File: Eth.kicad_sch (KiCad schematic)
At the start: 0 parts

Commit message: Eth güncellendi.
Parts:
- added C18, C19: 22pF, symbol Device:C
- added C20: 22uF, symbol Device:C
- added C21, C22, C23: 0.1uF, symbol Device:C
- added J2: RJ45_Hanrun_HR911105A_Horizontal, Connector_RJ:RJ45_Hanrun_HR911105A_Horizontal, symbol Connector:RJ45_Hanrun_HR911105A_Horizontal
- added R3: 10k, symbol Device:R
- added R4: 6.49k, symbol Device:R
- added U3: KSZ8081RNA, Package_DFN_QFN:QFN-24-1EP_4x4mm_P0.5mm_EP2.6x2.6mm, symbol Interface_Ethernet:KSZ8081RNA
- added Y1: Crystal, symbol Device:Crystal
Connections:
- new net: C22.1, J2.5 (RCT)
- new net: C18.1, U3.7 (XO), Y1.1
- new net: C23.1, J2.4 (TCT)
- new net: C19.1, U3.8 (XI), Y1.2
- new net: C20.2, C21.2, U3.1 (VDD_1.2)
- new net: J2.6 (RD-), U3.3 (RXM)
- new net: J2.3 (RD+), U3.4 (RXP)
- new net: J2.2 (TD-), U3.5 (TXM)
- new net: J2.1 (TD+), U3.6 (TXP)
- new net: R4.1, U3.9 (REXT)
- new net +3V3: R3.1
- new net ETH_CRS_DV: R3.2, U3.15 (CRS_DV/PHYAD[1:0])
- new net ETH_MDC: U3.11 (MDC)
- new net ETH_MDIO: U3.10 (MDIO)
- new net ETH_REF_CLK: U3.16 (REF_CLK)
- new net ETH_RXD0: U3.13 (RXD0)
- new net ETH_RXD1: U3.12 (RXD1)
- new net ETH_TXD0: U3.20 (TXD0)
- new net ETH_TXD1: U3.21 (TXD1)
- new net ETH_TXEN: U3.19 (TXEN)
- new net GND: C18.2, C19.2, C20.1, C21.1, C22.2, C23.2, R4.2, U3.22 (GND), U3.25 (GND)

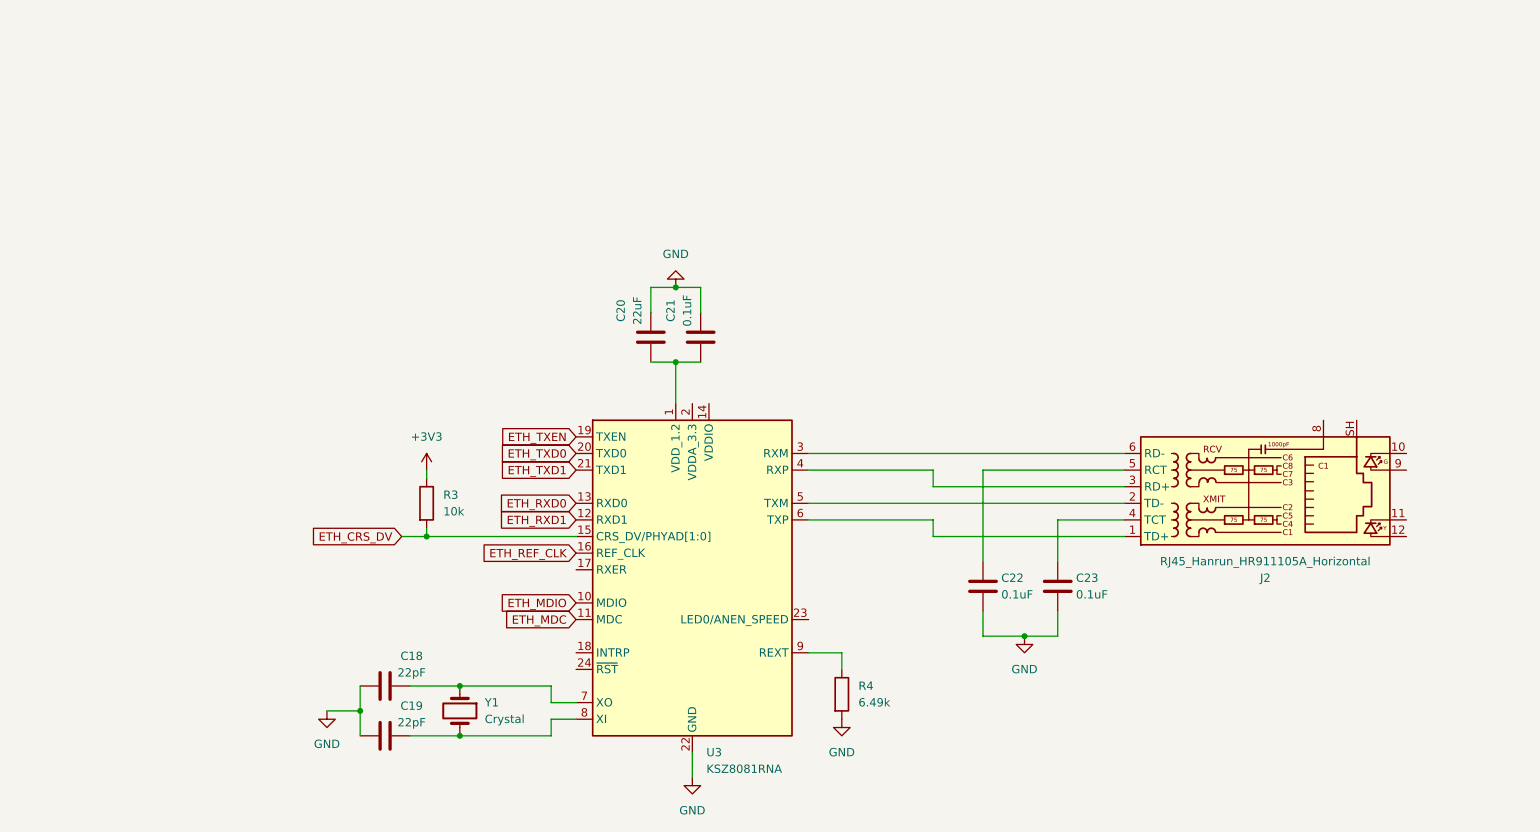
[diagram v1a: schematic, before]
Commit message: Eth güncellendi.
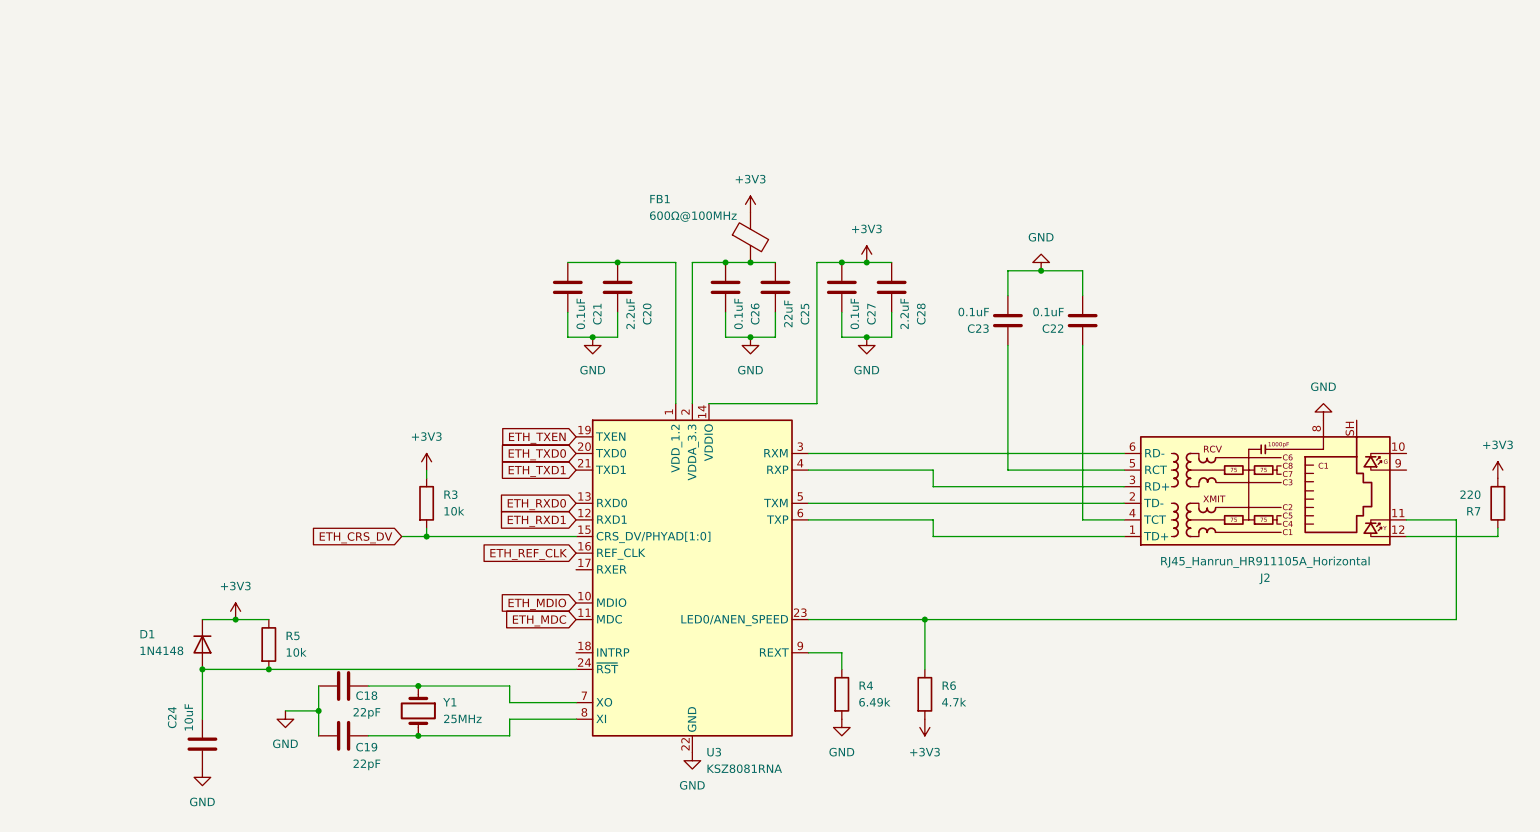
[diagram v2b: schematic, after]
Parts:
- added C24: 10uF, symbol Device:C
- added C25: 22uF, symbol Device:C
- added C26, C27: 0.1uF, symbol Device:C
- added C28: 2.2uF, symbol Device:C
- added D1: 1N4148, Diode_THT:D_DO-35_SOD27_P7.62mm_Horizontal, symbol Diode:1N4148
- added FB1: 600Ω@100MHz, symbol Device:FerriteBead
- added R5: 10k, symbol Device:R
- added R6: 4.7k, symbol Device:R
- added R7: 220, symbol Device:R
- C20: value 22uF -> 2.2uF
- Y1: value Crystal -> 25MHz
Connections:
- net +3V3: now also U3.14 (VDDIO), C27.2, C28.2, D1.1 (K), FB1.1, R5.1, R6.2, R7.2
- net GND: now also J2.8, C24.2, C25.1, C26.1, C27.1, C28.1
- net at C22.1: now also J2.4 (TCT); no longer J2.5 (RCT)
- net at C23.1: now also J2.5 (RCT); no longer J2.4 (TCT)
- net at U3.2 (VDDA_3.3): now also C25.2, C26.2, FB1.2
- net at U3.23 (LED0/ANEN_SPEED): now also J2.11, R6.1
- net at U3.24 (~{RST}): now also C24.1, D1.2 (A), R5.2
- net at J2.12: now also R7.1
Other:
- moved on the sheet: C18, C19, C20, C21, C22, C23, Y1

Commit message: Eth güncellendi.
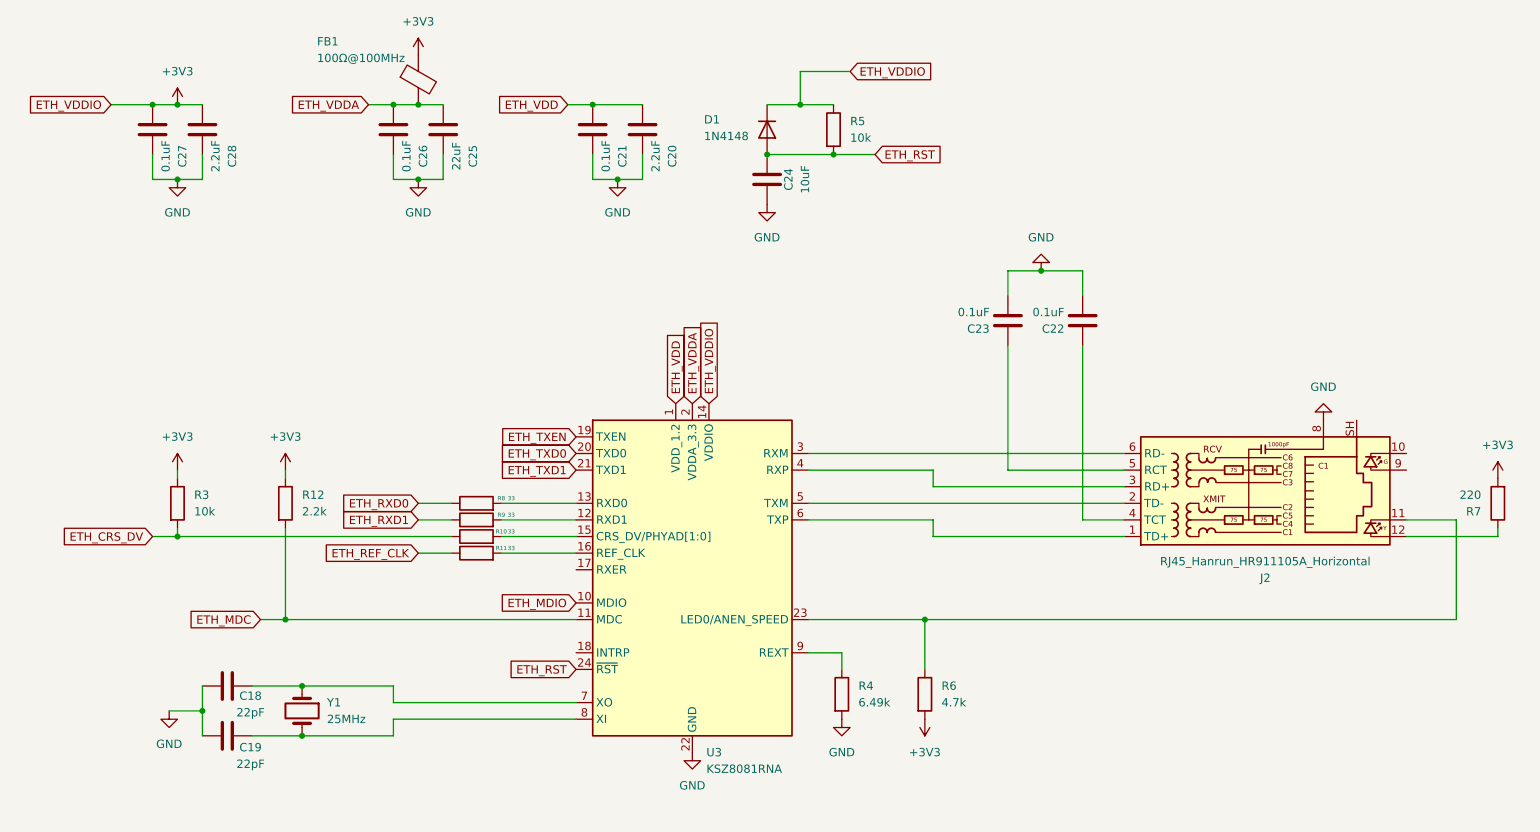
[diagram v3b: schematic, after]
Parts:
- added R10, R11, R8, R9: 33, symbol Device:R
- added R12: 2.2k, symbol Device:R
- FB1: value 600Ω@100MHz -> 100Ω@100MHz
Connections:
- net +3V3: now also R12.1
- net ETH_CRS_DV: now also R10.1; no longer U3.15 (CRS_DV/PHYAD[1:0])
- net ETH_MDC: now also R12.2
- net ETH_REF_CLK: now also R11.1; no longer U3.16 (REF_CLK)
- net ETH_RXD0: now also R8.1; no longer U3.13 (RXD0)
- net ETH_RXD1: now also R9.1; no longer U3.12 (RXD1)
- net ETH_VDDA: now reaches C25.2, C26.2, FB1.2, U3.2 (VDDA_3.3)
- net ETH_VDD: now reaches C20.2, C21.2, U3.1 (VDD_1.2)
- net ETH_RST: now reaches C24.1, D1.2 (A), R5.2, U3.24 (~{RST})
- new net: R9.2, U3.12 (RXD1)
- new net: R8.2, U3.13 (RXD0)
- new net: R10.2, U3.15 (CRS_DV/PHYAD[1:0])
- new net: R11.2, U3.16 (REF_CLK)
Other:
- moved on the sheet: C18, C19, R3, Y1

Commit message: Usb düzenlendi.
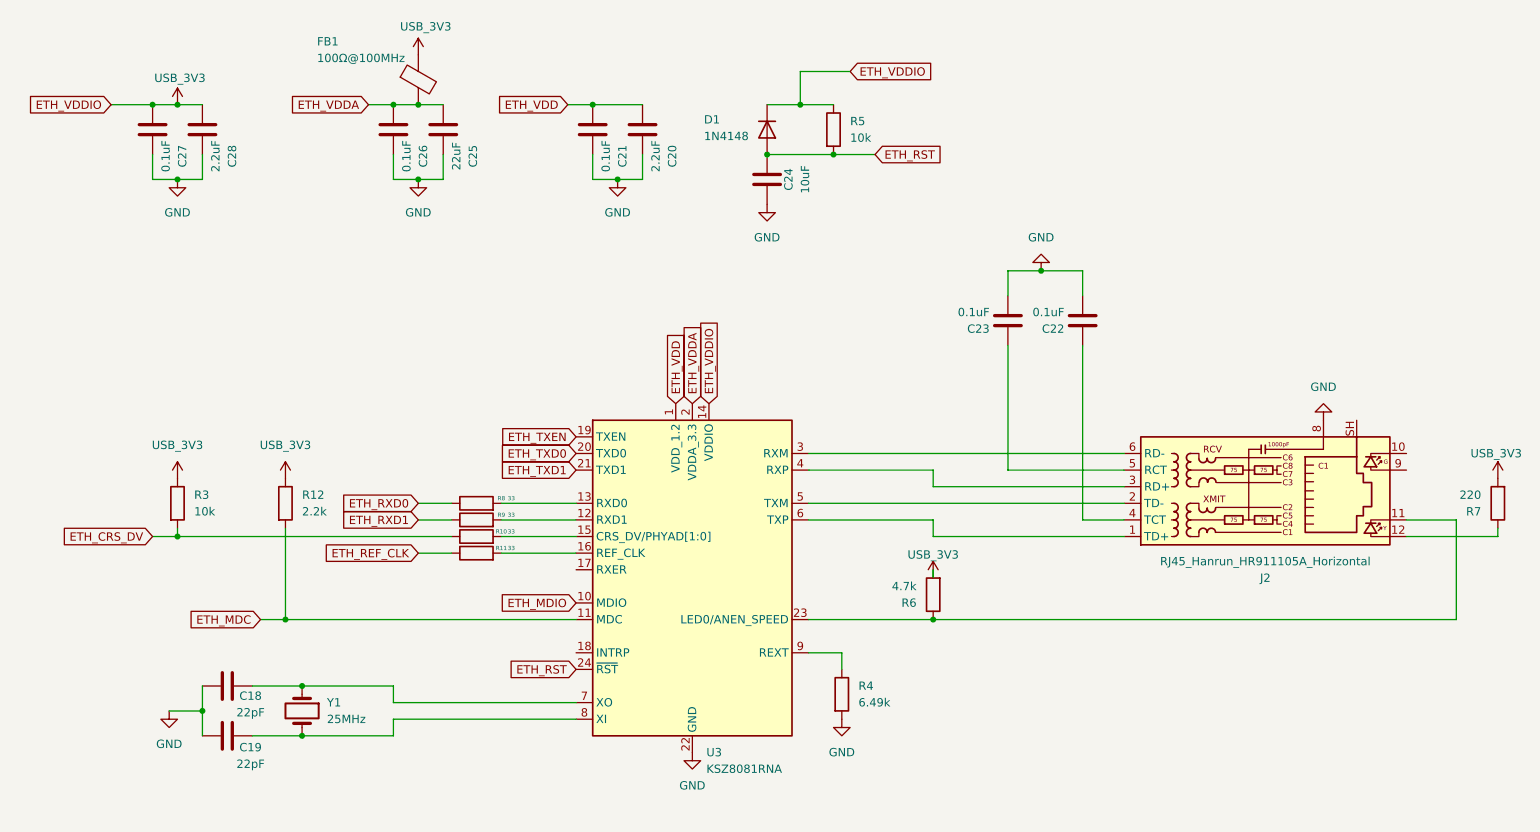
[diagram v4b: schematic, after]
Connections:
- net +3V3 renamed USB_3V3
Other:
- moved on the sheet: R6
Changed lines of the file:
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@@
 	)
 	(junction
-		(at 152.4 105.41)
+		(at 38.1 26.67)
 		(diameter 0)
 		(color 0 0 0 0)
 	)
 	(junction
-		(at 38.1 26.67)
+		(at 34.29 26.67)
 		(diameter 0)
 		(color 0 0 0 0)
 	)
 	(junction
-		(at 34.29 26.67)
+		(at 170.18 52.07)
 		(diameter 0)
 		(color 0 0 0 0)
 	)
 	(junction
-		(at 170.18 52.07)
+		(at 153.67 105.41)
 		(diameter 0)
 		(color 0 0 0 0)
@@
 	(wire
 		(pts
-			(xy 152.4 105.41) (xy 134.62 105.41)
-		)
-		(stroke
-			(width 0)
-			(type default)
-		)
-	)
-	(wire
-		(pts
 			(xy 134.62 110.49) (xy 139.7 110.49)
 		)
@@
 	(wire
 		(pts
+			(xy 153.67 99.06) (xy 153.67 97.79)
+		)
+		(stroke
+			(width 0)
+			(type default)
+		)
+	)
+	(wire
+		(pts
 			(xy 74.93 38.1) (xy 71.12 38.1)
 		)
@@
 	(wire
 		(pts
-			(xy 54.61 83.82) (xy 54.61 82.55)
-		)
-		(stroke
-			(width 0)
-			(type default)
-		)
-	)
-	(wire
-		(pts
-			(xy 38.1 83.82) (xy 38.1 82.55)
-		)
-		(stroke
-			(width 0)
-			(type default)
-		)
-	)
-	(wire
-		(pts
 			(xy 165.1 55.88) (xy 165.1 52.07)
 		)
@@
 	(wire
 		(pts
-			(xy 233.68 105.41) (xy 152.4 105.41)
+			(xy 134.62 105.41) (xy 153.67 105.41)
 		)
 		(stroke
@@
 	(wire
 		(pts
+			(xy 153.67 105.41) (xy 233.68 105.41)
+		)
+		(stroke
+			(width 0)
+			(type default)
+		)
+	)
+	(wire
+		(pts
 			(xy 176.53 55.88) (xy 176.53 52.07)
 		)
@@
 	(wire
 		(pts
-			(xy 152.4 113.03) (xy 152.4 105.41)
-		)
-		(stroke
-			(width 0)
-			(type default)
-		)
-	)
-	(wire
-		(pts
 			(xy 38.1 92.71) (xy 34.29 92.71)
 		)
@@
 	(symbol
 		(lib_id "Device:R")
-		(at 152.4 116.84 0)
+		(at 153.67 101.6 180)
 		(unit 1)
 		(body_style 1)
@@
 		(fields_autoplaced yes)
 		(property "Reference" "R6"
-			(at 154.94 115.5699 0)
+			(at 151.13 102.8701 0)
 			(show_name no)
 			(do_not_autoplace no)
@@
 		)
 		(property "Value" "4.7k"
-			(at 154.94 118.1099 0)
+			(at 151.13 100.3301 0)
 			(show_name no)
 			(do_not_autoplace no)
@@
 		)
 		(property "Footprint" ""
-			(at 150.622 116.84 90)
+			(at 155.448 101.6 90)
 			(hide yes)
 			(show_name no)
@@
 		)
 		(property "Datasheet" ""
-			(at 152.4 116.84 0)
+			(at 153.67 101.6 0)
 			(hide yes)
 			(show_name no)
@@
 		)
 		(property "Description" "Resistor"
-			(at 152.4 116.84 0)
+			(at 153.67 101.6 0)
 			(hide yes)
 			(show_name no)
@@
 	(symbol
 		(lib_id "power:+3V3")
-		(at 38.1 82.55 0)
+		(at 38.1 83.82 0)
 		(unit 1)
 		(body_style 1)
@@
 		(fields_autoplaced yes)
 		(property "Reference" "#PWR08"
-			(at 38.1 86.36 0)
+			(at 38.1 87.63 0)
 			(hide yes)
 			(show_name no)
@@
 			)
 		)
-		(property "Value" "+3V3"
-			(at 38.1 77.47 0)
+		(property "Value" "USB_3V3"
+			(at 38.1 78.74 0)
 			(show_name no)
 			(do_not_autoplace no)
@@
 		)
 		(property "Footprint" ""
-			(at 38.1 82.55 0)
+			(at 38.1 83.82 0)
 			(hide yes)
 			(show_name no)
@@
 		)
 		(property "Datasheet" ""
-			(at 38.1 82.55 0)
+			(at 38.1 83.82 0)
 			(hide yes)
 			(show_name no)
@@
 		)
 		(property "Description" "Power symbol creates a global label with name \"+3V3\""
-			(at 38.1 82.55 0)
+			(at 38.1 83.82 0)
 			(hide yes)
 			(show_name no)
@@
 		(in_pos_files yes)
 		(dnp no)
-		(fields_autoplaced yes)
 		(property "Reference" "#PWR016"
 			(at 240.03 87.63 0)
@@
 			)
 		)
-		(property "Value" "+3V3"
-			(at 240.03 78.74 0)
+		(property "Value" "USB_3V3"
+			(at 239.776 80.01 0)
 			(show_name no)
 			(do_not_autoplace no)
@@
 	(symbol
 		(lib_id "power:+3V3")
-		(at 152.4 120.65 180)
+		(at 153.67 99.06 0)
 		(unit 1)
 		(body_style 1)
@@
 		(in_pos_files yes)
 		(dnp no)
-		(fields_autoplaced yes)
 		(property "Reference" "#PWR017"
-			(at 152.4 116.84 0)
+			(at 153.67 102.87 0)
 			(hide yes)
 			(show_name no)
@@
 			)
 		)
-		(property "Value" "+3V3"
-			(at 152.4 125.73 0)
+		(property "Value" "USB_3V3"
+			(at 153.67 95.504 0)
 			(show_name no)
 			(do_not_autoplace no)
@@
 		)
 		(property "Footprint" ""
-			(at 152.4 120.65 0)
+			(at 153.67 99.06 0)
 			(hide yes)
 			(show_name no)
@@
 		)
 		(property "Datasheet" ""
-			(at 152.4 120.65 0)
+			(at 153.67 99.06 0)
 			(hide yes)
 			(show_name no)
@@
 		)
 		(property "Description" "Power symbol creates a global label with name \"+3V3\""
-			(at 152.4 120.65 0)
+			(at 153.67 99.06 0)
 			(hide yes)
 			(show_name no)
@@
 		(in_pos_files yes)
 		(dnp no)
-		(fields_autoplaced yes)
 		(property "Reference" "#PWR021"
 			(at 38.1 30.48 0)
@@
 			)
 		)
-		(property "Value" "+3V3"
-			(at 38.1 21.59 0)
+		(property "Value" "USB_3V3"
+			(at 34.544 22.606 0)
 			(show_name no)
 			(do_not_autoplace no)
@@
 					(size 1.27 1.27)
 				)
+				(justify left)
 			)
 		)
@@
 	(symbol
 		(lib_id "power:+3V3")
-		(at 54.61 82.55 0)
+		(at 54.61 83.82 0)
 		(unit 1)
 		(body_style 1)
@@
 		(fields_autoplaced yes)
 		(property "Reference" "#PWR023"
-			(at 54.61 86.36 0)
+			(at 54.61 87.63 0)
 			(hide yes)
 			(show_name no)
@@
 			)
 		)
-		(property "Value" "+3V3"
-			(at 54.61 77.47 0)
+		(property "Value" "USB_3V3"
+			(at 54.61 78.74 0)
 			(show_name no)
 			(do_not_autoplace no)
@@
 		)
 		(property "Footprint" ""
-			(at 54.61 82.55 0)
+			(at 54.61 83.82 0)
 			(hide yes)
 			(show_name no)
@@
 		)
 		(property "Datasheet" ""
-			(at 54.61 82.55 0)
+			(at 54.61 83.82 0)
 			(hide yes)
 			(show_name no)
@@
 		)
 		(property "Description" "Power symbol creates a global label with name \"+3V3\""
-			(at 54.61 82.55 0)
+			(at 54.61 83.82 0)
 			(hide yes)
 			(show_name no)
@@
 		(in_pos_files yes)
 		(dnp no)
-		(fields_autoplaced yes)
 		(property "Reference" "#PWR018"
 			(at 74.93 22.86 0)
@@
 			)
 		)
-		(property "Value" "+3V3"
-			(at 74.93 13.97 0)
+		(property "Value" "USB_3V3"
+			(at 72.136 14.732 0)
 			(show_name no)
 			(do_not_autoplace no)
@@
 					(size 1.27 1.27)
 				)
+				(justify left)
 			)
 		)
